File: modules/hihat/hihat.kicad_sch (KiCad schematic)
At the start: 57 parts, among them U1 VTL5C, U2 MCP6002-xSN, U3 MCP6002-xSN, U4 MCP6002-xSN, U5 ATtiny1616-M

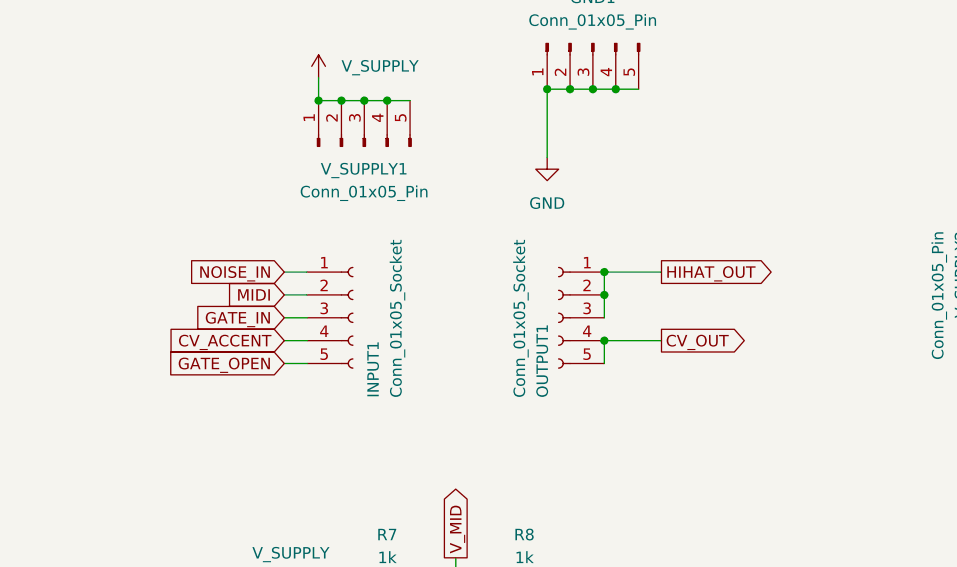
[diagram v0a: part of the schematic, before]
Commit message: hihat: Add MIDI THRU support
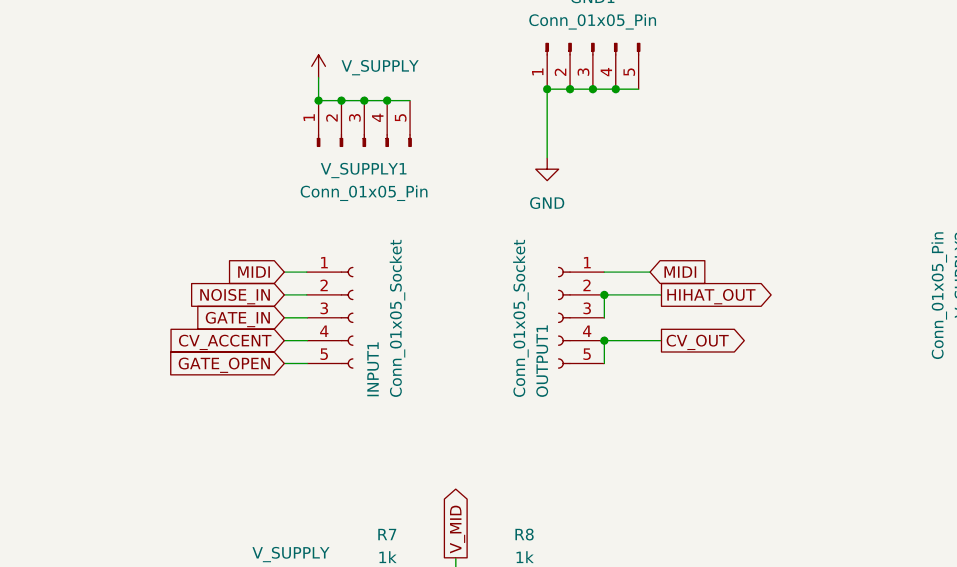
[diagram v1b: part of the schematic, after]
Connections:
- net HIHAT_OUT: no longer OUTPUT1.1 (Pin_1)
- net MIDI: now also INPUT1.1 (Pin_1), OUTPUT1.1 (Pin_1); no longer INPUT1.2 (Pin_2)
- net NOISE_IN: now also INPUT1.2 (Pin_2); no longer INPUT1.1 (Pin_1)
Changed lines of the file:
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@@
-	)
-	(junction
-		(at 379.73 50.8)
-		(diameter 0)
-		(color 0 0 0 0)
 	)
 	(junction
@@
 	)
 	(junction
+		(at 379.73 53.34)
+		(diameter 0)
+		(color 0 0 0 0)
+	)
+	(junction
 		(at 381 30.48)
 		(diameter 0)
@@
 	)
 	(junction
-		(at 379.73 53.34)
-		(diameter 0)
-		(color 0 0 0 0)
-	)
-	(junction
 		(at 69.85 81.28)
 		(diameter 0)
@@
 	(wire
 		(pts
+			(xy 344.17 53.34) (xy 346.71 53.34)
+		)
+		(stroke
+			(width 0)
+			(type default)
+		)
+	)
+	(wire
+		(pts
 			(xy 316.23 128.27) (xy 316.23 130.81)
 		)
@@
 	(wire
 		(pts
+			(xy 379.73 53.34) (xy 386.08 53.34)
+		)
+		(stroke
+			(width 0)
+			(type default)
+		)
+	)
+	(wire
+		(pts
 			(xy 83.82 81.28) (xy 92.71 81.28)
 		)
@@
 	(wire
 		(pts
+			(xy 27.94 297.18) (xy 27.94 298.45)
+		)
+		(stroke
+			(width 0)
+			(type default)
+		)
+	)
+	(wire
+		(pts
+			(xy 347.98 102.87) (xy 347.98 107.95)
+		)
+		(stroke
+			(width 0)
+			(type default)
+		)
+	)
+	(wire
+		(pts
+			(xy 237.49 201.93) (xy 250.19 201.93)
+		)
+		(stroke
+			(width 0)
+			(type default)
+		)
+	)
+	(wire
+		(pts
+			(xy 228.6 101.6) (xy 228.6 104.14)
+		)
+		(stroke
+			(width 0)
+			(type default)
+		)
+	)
+	(wire
+		(pts
+			(xy 326.39 113.03) (xy 326.39 109.22)
+		)
+		(stroke
+			(width 0)
+			(type default)
+		)
+	)
+	(wire
+		(pts
+			(xy 107.95 101.6) (xy 115.57 101.6)
+		)
+		(stroke
+			(width 0)
+			(type default)
+		)
+	)
+	(wire
+		(pts
+			(xy 358.14 119.38) (xy 358.14 127)
+		)
+		(stroke
+			(width 0)
+			(type default)
+		)
+	)
+	(wire
+		(pts
+			(xy 381 30.48) (xy 383.54 30.48)
+		)
+		(stroke
+			(width 0)
+			(type default)
+		)
+	)
+	(wire
+		(pts
+			(xy 100.33 101.6) (xy 82.55 101.6)
+		)
+		(stroke
+			(width 0)
+			(type default)
+		)
+	)
+	(wire
+		(pts
+			(xy 107.95 215.9) (xy 107.95 222.25)
+		)
+		(stroke
+			(width 0)
+			(type default)
+		)
+	)
+	(wire
+		(pts
+			(xy 316.23 184.15) (xy 316.23 171.45)
+		)
+		(stroke
+			(width 0)
+			(type default)
+		)
+	)
+	(wire
+		(pts
+			(xy 129.54 208.28) (xy 137.16 208.28)
+		)
+		(stroke
+			(width 0)
+			(type default)
+		)
+	)
+	(wire
+		(pts
+			(xy 363.22 82.55) (xy 363.22 86.36)
+		)
+		(stroke
+			(width 0)
+			(type default)
+		)
+	)
+	(wire
+		(pts
 			(xy 344.17 50.8) (xy 346.71 50.8)
 		)
@@
 	(wire
 		(pts
-			(xy 27.94 297.18) (xy 27.94 298.45)
-		)
-		(stroke
-			(width 0)
-			(type default)
-		)
-	)
-	(wire
-		(pts
-			(xy 347.98 102.87) (xy 347.98 107.95)
-		)
-		(stroke
-			(width 0)
-			(type default)
-		)
-	)
-	(wire
-		(pts
-			(xy 237.49 201.93) (xy 250.19 201.93)
-		)
-		(stroke
-			(width 0)
-			(type default)
-		)
-	)
-	(wire
-		(pts
-			(xy 228.6 101.6) (xy 228.6 104.14)
-		)
-		(stroke
-			(width 0)
-			(type default)
-		)
-	)
-	(wire
-		(pts
-			(xy 326.39 113.03) (xy 326.39 109.22)
-		)
-		(stroke
-			(width 0)
-			(type default)
-		)
-	)
-	(wire
-		(pts
-			(xy 107.95 101.6) (xy 115.57 101.6)
-		)
-		(stroke
-			(width 0)
-			(type default)
-		)
-	)
-	(wire
-		(pts
-			(xy 358.14 119.38) (xy 358.14 127)
-		)
-		(stroke
-			(width 0)
-			(type default)
-		)
-	)
-	(wire
-		(pts
-			(xy 381 30.48) (xy 383.54 30.48)
-		)
-		(stroke
-			(width 0)
-			(type default)
-		)
-	)
-	(wire
-		(pts
-			(xy 100.33 101.6) (xy 82.55 101.6)
-		)
-		(stroke
-			(width 0)
-			(type default)
-		)
-	)
-	(wire
-		(pts
-			(xy 107.95 215.9) (xy 107.95 222.25)
-		)
-		(stroke
-			(width 0)
-			(type default)
-		)
-	)
-	(wire
-		(pts
-			(xy 316.23 184.15) (xy 316.23 171.45)
-		)
-		(stroke
-			(width 0)
-			(type default)
-		)
-	)
-	(wire
-		(pts
-			(xy 129.54 208.28) (xy 137.16 208.28)
-		)
-		(stroke
-			(width 0)
-			(type default)
-		)
-	)
-	(wire
-		(pts
-			(xy 363.22 82.55) (xy 363.22 86.36)
-		)
-		(stroke
-			(width 0)
-			(type default)
-		)
-	)
-	(wire
-		(pts
 			(xy 363.22 86.36) (xy 367.03 86.36)
 		)
@@
 	(wire
 		(pts
+			(xy 379.73 50.8) (xy 384.81 50.8)
+		)
+		(stroke
+			(width 0)
+			(type default)
+		)
+	)
+	(wire
+		(pts
 			(xy 322.58 163.83) (xy 322.58 160.02)
 		)
@@
 	(wire
 		(pts
+			(xy 379.73 53.34) (xy 379.73 55.88)
+		)
+		(stroke
+			(width 0)
+			(type default)
+		)
+	)
+	(wire
+		(pts
 			(xy 100.33 222.25) (xy 107.95 222.25)
 		)
@@
 	(wire
 		(pts
-			(xy 344.17 53.34) (xy 346.71 53.34)
-		)
-		(stroke
-			(width 0)
-			(type default)
-		)
-	)
-	(wire
-		(pts
 			(xy 154.94 165.1) (xy 132.08 165.1)
 		)
@@
 	(wire
 		(pts
-			(xy 379.73 50.8) (xy 379.73 53.34)
-		)
-		(stroke
-			(width 0)
-			(type default)
-		)
-	)
-	(wire
-		(pts
 			(xy 316.23 125.73) (xy 316.23 128.27)
 		)
@@
 	(wire
 		(pts
-			(xy 379.73 50.8) (xy 386.08 50.8)
-		)
-		(stroke
-			(width 0)
-			(type default)
-		)
-	)
-	(wire
-		(pts
 			(xy 107.95 165.1) (xy 104.14 165.1)
 		)
@@
 		(pts
 			(xy 246.38 76.2) (xy 252.73 76.2)
-		)
-		(stroke
-			(width 0)
-			(type default)
-		)
-	)
-	(wire
-		(pts
-			(xy 379.73 53.34) (xy 379.73 55.88)
 		)
 		(stroke
@@
 	(global_label "MIDI"
 		(shape input)
-		(at 344.17 53.34 180)
+		(at 344.17 50.8 180)
 		(fields_autoplaced yes)
 		(effects
@@
 		)
 		(property "Intersheetrefs" "${INTERSHEET_REFS}"
-			(at 337.2538 53.34 0)
+			(at 337.2538 50.8 0)
 			(effects
 				(font
@@
 		)
 	)
+	(global_label "MIDI"
+		(shape input)
+		(at 384.81 50.8 0)
+		(fields_autoplaced yes)
+		(effects
+			(font
+				(size 1.27 1.27)
+			)
+			(justify left)
+		)
+		(property "Intersheetrefs" "${INTERSHEET_REFS}"
+			(at 391.7262 50.8 0)
+			(effects
+				(font
+					(size 1.27 1.27)
+				)
+				(justify left)
+				(hide yes)
+			)
+		)
+	)
 	(global_label "TX"
 		(shape output)
@@
 	(global_label "HIHAT_OUT"
 		(shape output)
-		(at 386.08 50.8 0)
-		(fields_autoplaced yes)
-		(effects
-			(font
-				(size 1.27 1.27)
-			)
-			(justify left)
-		)
-		(property "Intersheetrefs" "${INTERSHEET_REFS}"
-			(at 398.9834 50.8 0)
+		(at 386.08 53.34 0)
+		(fields_autoplaced yes)
+		(effects
+			(font
+				(size 1.27 1.27)
+			)
+			(justify left)
+		)
+		(property "Intersheetrefs" "${INTERSHEET_REFS}"
+			(at 398.9834 53.34 0)
 			(effects
 				(font
@@
 	(global_label "NOISE_IN"
 		(shape input)
-		(at 344.17 50.8 180)
+		(at 344.17 53.34 180)
 		(fields_autoplaced yes)
 		(effects
@@
 		)
 		(property "Intersheetrefs" "${INTERSHEET_REFS}"
-			(at 332.6576 50.8 0)
-			(effects
-				(font
+			(at 332.6576 53.34 0)
+			(effects
+				(font
